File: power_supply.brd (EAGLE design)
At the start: 160 x 100 mm, 26 parts, among them IC3 LM317

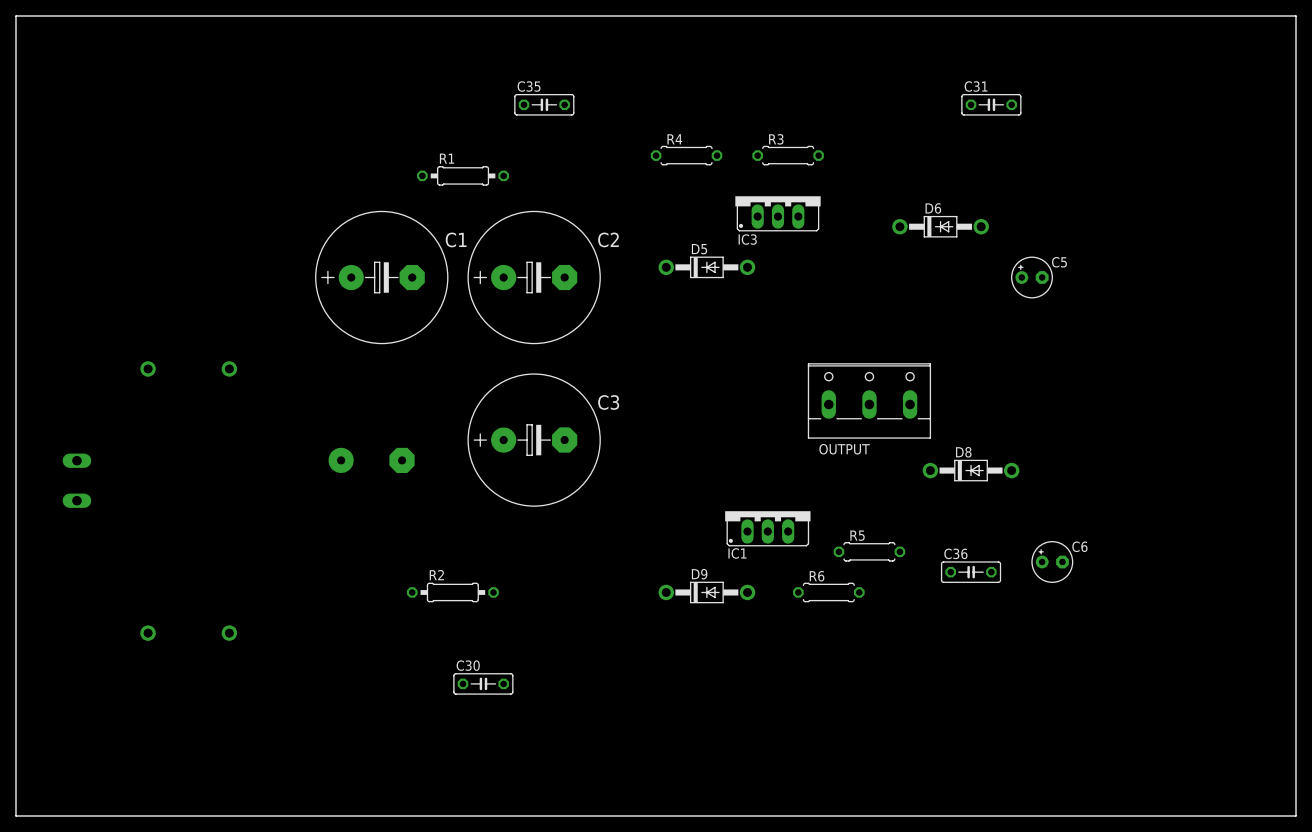
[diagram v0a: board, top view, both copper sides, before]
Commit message: Fuente posicionada 20%
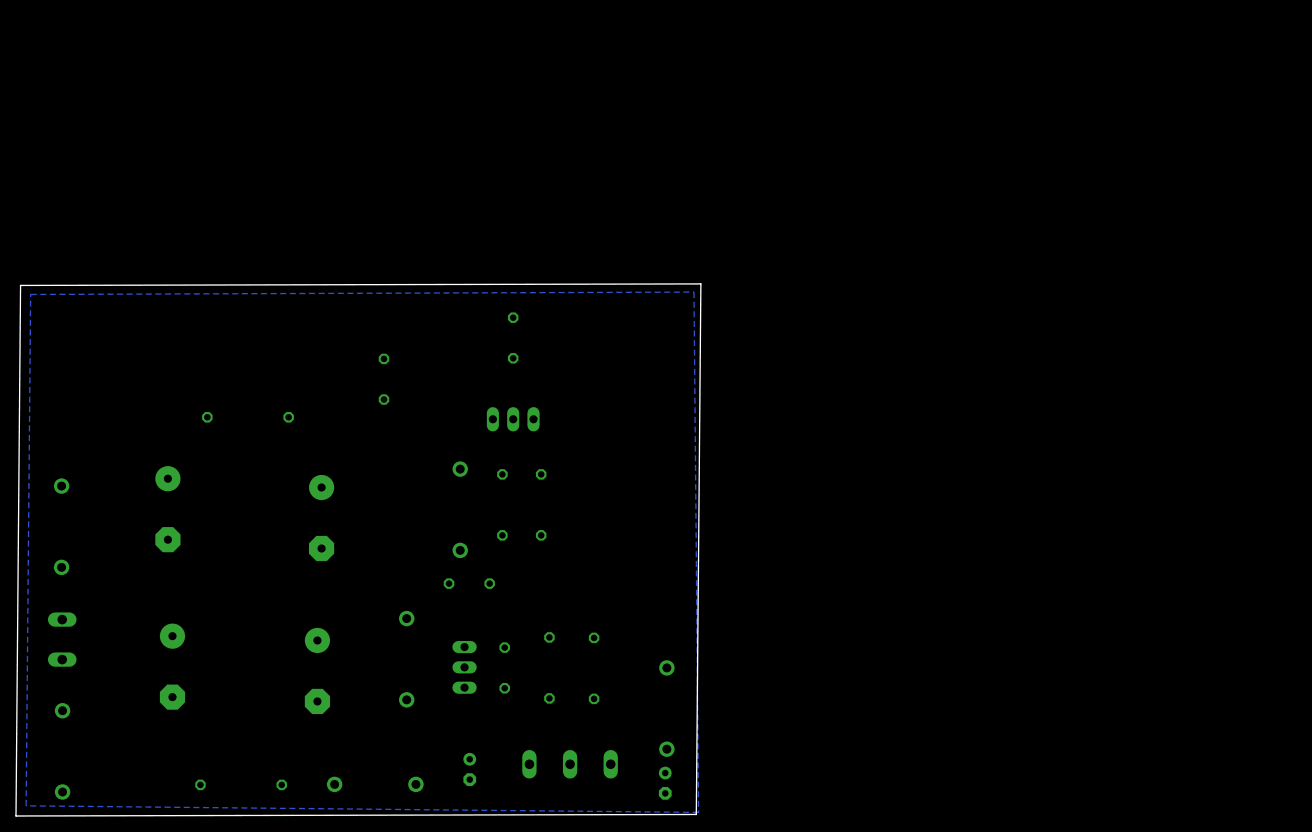
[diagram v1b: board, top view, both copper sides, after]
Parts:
- moved D8 84.2 mm to (44.9, 3.95), flipped to the bottom, turned to 180 degrees
- moved C5 78.1 mm to (81.2, 4.10), flipped to the bottom, turned to 270 degrees
- moved C6 77.3 mm to (56.7, 5.82), flipped to the bottom, turned to 270 degrees
- moved D6 69.3 mm to (81.4, 13.4), flipped to the bottom, turned to 90 degrees
- moved C31 66.5 mm to (62.1, 59.8), flipped to the bottom, turned to 90 degrees
- moved C35 60.6 mm to (56.7, 29.1), flipped to the bottom
- moved C36 59.5 mm to (61.1, 18.5), flipped to the bottom, turned to 270 degrees
- moved OUTPUT 59.5 mm to (69.3, 5.83), flipped to the bottom, turned to 180 degrees
- moved R3 56.4 mm to (60.8, 38.9), flipped to the bottom, turned to 270 degrees
- moved R4 47.3 mm to (65.7, 38.9), flipped to the bottom, turned to 90 degrees
- moved IC1 44.9 mm to (53.5, 18.6), flipped to the bottom, turned to 270 degrees
- moved D5 43.2 mm to (55.5, 38.3), flipped to the bottom, turned to 270 degrees
- moved IC3 41.7 mm to (62.1, 52.1), flipped to the bottom
- moved R1 40.4 mm to (29.0, 49.8), flipped to the bottom, turned to 180 degrees
- moved C2 40.1 mm to (38.2, 37.2), flipped to the bottom, turned to 270 degrees
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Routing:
- added copper zone on layer 16, net AGND
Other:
- board size 160 x 100 mm -> 85.6 x 66.5 mm
